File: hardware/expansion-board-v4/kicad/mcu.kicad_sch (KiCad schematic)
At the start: 28 parts, among them J4 USB-C_16P, SW1 RESET短接焊盘, SW2 BOOTSEL短接焊盘, U8 RP2040, U9 W25Q128JVSIQ, Y1 12MHz

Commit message: feat(hw): 删掉 TP1-7 与 SW1，飞线交叉 834→612、B 面中间让给电池
判据不是「省地方」，是这 7 条网络除了测试点没有第三方节点：
DEMOD0-3(GPIO20-23) 和 RECOVERED_CLK(GPIO24) 是固件里 PIO 解码状态机
往外**输出**的调试信号，不在接收链上——接收链是
AD8319 → TLV3501 比较器 → PULSES → GPIO19，一个测试点都没有。

固件调试在已打样的 v3.2 上做，那块板的 TP 和解调链与本板逐条相同
（expansion-board-v3/tools/sheet_mcu.py:95）。刷机走 USB UF2，
SWD 不是烧录必需。

SW1(RESET) 一并删掉：RUN 脚由 R5 上拉即可，复位靠断电或软件。

保留 SW2 并已搬到 U8 与 U9 之间——它是唯一的强制刷机入口，而且挂在
QSPI_SS 这条 RP2040 到 Flash 的片选线上，原来在 x52.8 等于给总线挂了
36mm stub（QSPI_SCLK 全长才 7.4mm），现在 6.1mm。

  飞线总长  3100 → 2640mm  (-15%)
  飞线交叉   834 → 612 处  (-27%)
  元件数     182 → 174
  B 面中间   完整让给电池 955465 (65x54)

GPIO20-24 的网络名保留在引脚映射表里没标 NC，将来要加回测试点补一句
s.place 即可，原理图上也还看得出这几个脚的预期用途。

验收：DRC error 0 条，F 面丝印全通过，原理图与 PCB 元件集合一致
（差集只有 H1-H4 螺丝孔），覆铜已重填。
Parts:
- removed SW1: RESET短接焊盘, Jumper:SolderJumper-2_P1.3mm_Open_Pad1.0x1.5mm, symbol Jumper:SolderJumper_2_Open
- removed TP1, TP2, TP3, TP4, TP5, TP6, TP7: TestPoint, TestPoint:TestPoint_Pad_1.0x1.0mm, symbol Connector:TestPoint

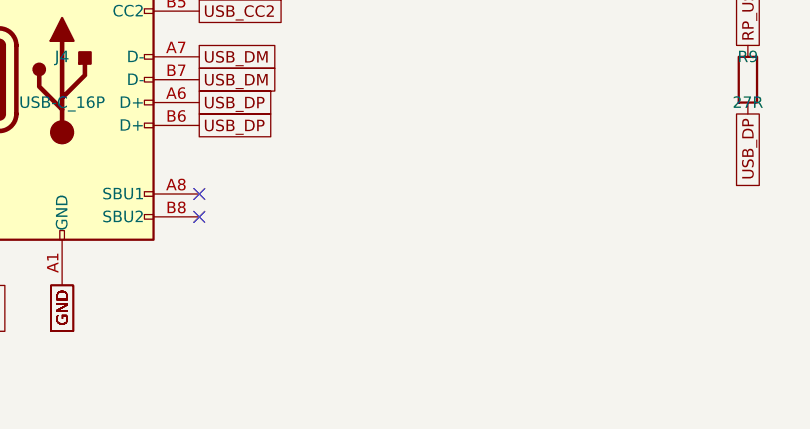
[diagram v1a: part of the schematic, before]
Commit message: feat(hw): 实现「单面可用」——J4 移 F 面、补 CC 下拉、电源电容改封装
## 单面可用是保底

不带电源版的 B 面现在**零贴装件**，可以走嘉立创经济型单面（¥267.1），
不必被迫上标准型双面（¥614.96）。上一版把 J4 留在 B 面，等于不带电源版
还是双面，只省 ¥35，白做。

三个改动：

  J4 (USB-C) → F 面 (144.63,73.00) rot=0
      courtyard 右沿贴齐板边 150，开口仍朝 +X（与微雪 H1 同侧）。
      翻面会镜像 x 且 USB-C 封装原点不在几何中心，x 是重新解出来的。
      USB_DP/DM 连的 R9/R10 本来就在 F 面 x117，搬过去走线反而更短；
      USB_CC1/2 与 USB_VBUS 只有带电源版才用，跨面过孔即可。

  新增 R7/R8（5.1k CC 下拉）→ F 面，紧邻 J4 2.2mm
      不带电源版没有 CH224K，CC 悬空则主机根本不认设备——USB-C 规范要求
      device 端呈现 Rd 才会被检测和枚举，不枚举就没法 UF2 刷机。
      **与 CH224K 二选一**，带电源版不贴。

  R37 (138.80,69.84) → (137.75,70.75)
      J4 的通孔安装脚穿到 B 面，落进了 R37 的 courtyard（DRC 报
      pth_inside_courtyard）。顺带把它到 CH224K CFG1 脚的距离 2.97→2.56mm。

## 电源电容改封装

不是为散热——电阻功率算过，最大的 R43 也才 (9−3.3)²/1k = 32.5mW，
0603 有 3 倍余量。真正的理由是两条：

  C72  6.8µF/25V  0603 → 1206
      接 PD 诱骗后的 9V 侧，耐压不能降。而 0603 在 25V 档容值上限只有
      1~2.2µF，6.8µF/25V 根本买不到。换封装后原位撞 C80，已就近重贴
      （按「离同网芯片引脚最近」而不是「离原位最近」找的位）。

  C73/C74/C75  10µF  0603 → 0805
      直流偏置下的容值衰减：10µF/16V X5R 在 5V 偏压下，0603 只剩
      3~4µF(−60%)，0805 还有 6~7µF(−30%)，直接影响输出纹波。

## 新增电源采购 CSV（单独一份，不混进整板 xlsx）

tools/gen_power_csv.py → BOM_电源采购_淘宝.csv，22 种料 / 30 颗。
按「卖家怎么找货」分组，同规格合并给总数，备注写清耐压/精度/为什么
封装不能换，末尾附两个版本的贴装差异。整板 88 料号的 xlsx 发给卖家太乱。

验收：DRC error 0 条，F 面丝印全通过，原理图↔PCB 零不一致，
176 元件已固化，全套文档重生成（BOM 88 料号 / SMT 79 料号 164 贴片位）。
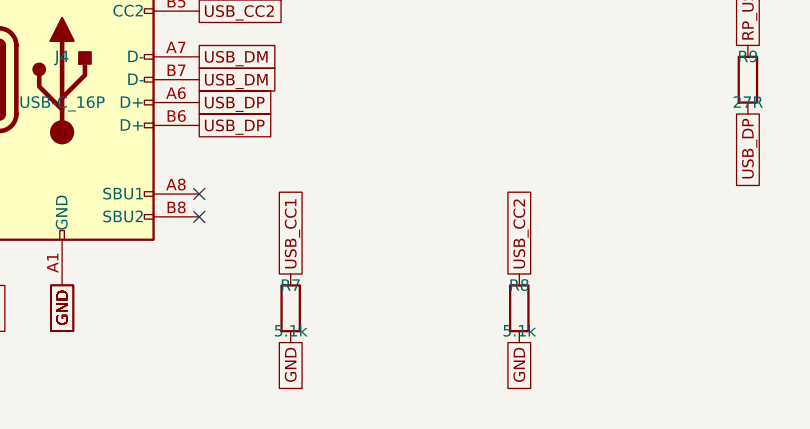
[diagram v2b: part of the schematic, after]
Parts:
- added R7, R8: 5.1k, Resistor_SMD:R_0603_1608Metric, symbol Device:R
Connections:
- net GND: now also R7.2, R8.2
- net USB_CC1: now also R7.1
- net USB_CC2: now also R8.1
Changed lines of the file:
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@@
+	(symbol
+		(lib_id "Device:R")
+		(at 88.9 215.9 0)
+		(unit 1)
+		(exclude_from_sim no)
+		(in_bom yes)
+		(on_board yes)
+		(dnp no)
+		(property "Reference" "R7"
+			(at 88.9 213.36 0)
+			(effects (font (size 1.27 1.27)))
+		)
+		(property "Value" "5.1k"
+			(at 88.9 218.44 0)
+			(effects (font (size 1.27 1.27)))
+		)
+		(property "Footprint" "Resistor_SMD:R_0603_1608Metric"
+			(at 88.9 220.98 0)
+			(effects (font (size 1.27 1.27))
+				(hide yes))
+		)
+		(property "Datasheet" "~"
+			(at 88.9 223.52 0)
+			(effects (font (size 1.27 1.27))
+				(hide yes))
+		)
+		(pin "1"
+		)
+		(pin "2"
+		)
+		(instances
+			(project "expansion-board-v4"
+				(path "/10000000-0000-4000-8000-000000000001/20000000-0000-4000-8000-000000000002"
+					(reference "R7")
+					(unit 1)
+				)
+			)
+		)
+	)
+	(global_label "USB_CC1"
+		(shape passive)
+		(at 88.9 212.09 270)
+		(effects (font (size 1.27 1.27)) (justify left))
+	)
+	(global_label "GND"
+		(shape passive)
+		(at 88.9 219.71 90)
+		(effects (font (size 1.27 1.27)) (justify right))
+	)
+	(symbol
+		(lib_id "Device:R")
+		(at 114.3 215.9 0)
+		(unit 1)
+		(exclude_from_sim no)
+		(in_bom yes)
+		(on_board yes)
+		(dnp no)
+		(property "Reference" "R8"
+			(at 114.3 213.36 0)
+			(effects (font (size 1.27 1.27)))
+		)
+		(property "Value" "5.1k"
+			(at 114.3 218.44 0)
+			(effects (font (size 1.27 1.27)))
+		)
+		(property "Footprint" "Resistor_SMD:R_0603_1608Metric"
+			(at 114.3 220.98 0)
+			(effects (font (size 1.27 1.27))
+				(hide yes))
+		)
+		(property "Datasheet" "~"
+			(at 114.3 223.52 0)
+			(effects (font (size 1.27 1.27))
+				(hide yes))
+		)
+		(pin "1"
+		)
+		(pin "2"
+		)
+		(instances
+			(project "expansion-board-v4"
+				(path "/10000000-0000-4000-8000-000000000001/20000000-0000-4000-8000-000000000002"
+					(reference "R8")
+					(unit 1)
+				)
+			)
+		)
+	)
+	(global_label "USB_CC2"
+		(shape passive)
+		(at 114.3 212.09 270)
+		(effects (font (size 1.27 1.27)) (justify left))
+	)
+	(global_label "GND"
+		(shape passive)
+		(at 114.3 219.71 90)
+		(effects (font (size 1.27 1.27)) (justify right))
+	)
 	(symbol
 		(lib_id "Device:R")

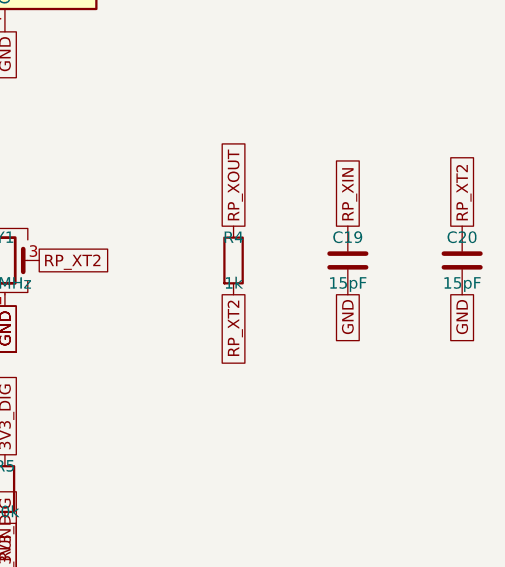
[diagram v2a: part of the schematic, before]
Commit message: fix(v4): 晶振负载电容按实测 CL 重算——C19/C20→33pF，C68/C69→18pF
罩哥给出实际买到的三颗晶振型号，CL 全部查实：

    Y1  X322512MSB4SI              CL=20pF     立创/JLCPCB/Evelta 三处一致
    Y2  ABM8W-48.0000MHZ-7-D1X-T3  CL=7pF      型号里的「-7-」就是 CL
    Y3  Q13FC13500004 (FC-135)     CL=12.5pF   Epson 官方 IC 配套页

按 C = (CL − Cstray) × 2、Cstray 取 3pF 重算：

              原值          新值      原偏差              新偏差
    C19/C20   15/15pF   →   33/33pF   -9.50pF ≈ 95ppm    -0.50pF ≈ 5ppm
    C68/C69   12/15pF   →   18/18pF   -2.83pF ≈ 28ppm    -0.50pF ≈ 5ppm
                            ↑ 原值还**不对称**，降低起振裕度

Y3 的 28ppm ≈ RTC 每天走时差 2.4 秒；改后 0.43 秒。
Y1 的 95ppm 虽在 USB 全速 ±500ppm 内，但计时精度白损失一个数量级。
sheet_subghz.py 里原注释写着「32k 12/15pF 照抄」——就是照抄参考设计没算。

Y2 不需要外部负载电容（CC1312 片内电容阵列），但 CL=7pF 要在固件 CCFG 的
XOSC HF cap-array 里配，这是软件项，已在核对清单里标注。

## 验证过：Gerber 一个字节没变

value 字段在 F.Fab 层，位号在 F.Silkscreen 层，导出的 13 层不含 F.Fab。
逐文件比对（排除 CreationDate/ProjectId 等注释行）：
**15 个 Gerber/钻孔文件的图形指令完全一致，0 处差异**。已打样的文件不用重发。

## 🔴 顺带修了一个静默的缓存 bug

_fresh_netlist() 只比对顶层 expansion-board-v4.kicad_sch 的 mtime，
而元件都在 mcu/power/rf1090/sensors/subghz/interface 这些**子页**里。
改子页时顶层 mtime 不动 → 缓存判定"新鲜" → 拿旧网表出文档，**一声不吭**。

实测：子页改于 23:56，网表缓存停在 8-26 19:13，顶层原理图是 8-26 15:52
（比缓存还旧）。结果原理图和板子都更新了，BOM_PURCHASE.md 和 ASSEMBLY.md
却还印着 12pF/15pF。

改成比对**所有 .kicad_sch 的最新 mtime**。四个脚本都有这个函数，一并修了。
这跟 2026-08-23 那次 /tmp 缓存是同一类问题的第二种形态——上次修了"只判存在性
不判时间戳"，这次是"判了时间戳但判错了对象"。

gen_bom.py 的 PARTS 断言拦住了新值未归类，正是它该干的活。
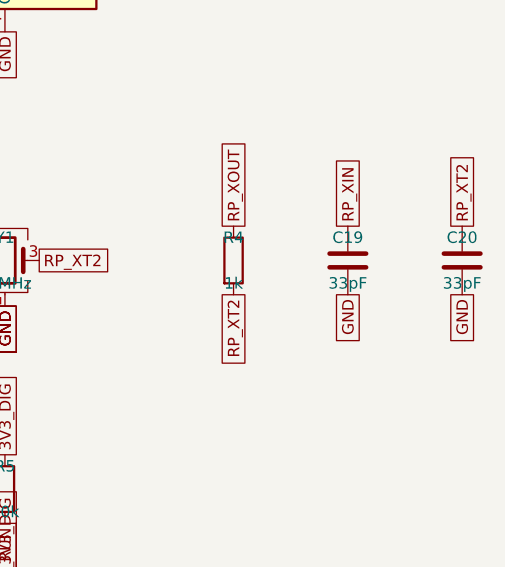
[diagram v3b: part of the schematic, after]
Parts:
- C19, C20: value 15pF -> 33pF
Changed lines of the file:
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@@
 			(effects (font (size 1.27 1.27)))
 		)
-		(property "Value" "15pF"
+		(property "Value" "33pF"
 			(at 228.6 116.84 0)
 			(effects (font (size 1.27 1.27)))
@@
 			(effects (font (size 1.27 1.27)))
 		)
-		(property "Value" "15pF"
+		(property "Value" "33pF"
 			(at 241.3 116.84 0)
 			(effects (font (size 1.27 1.27)))

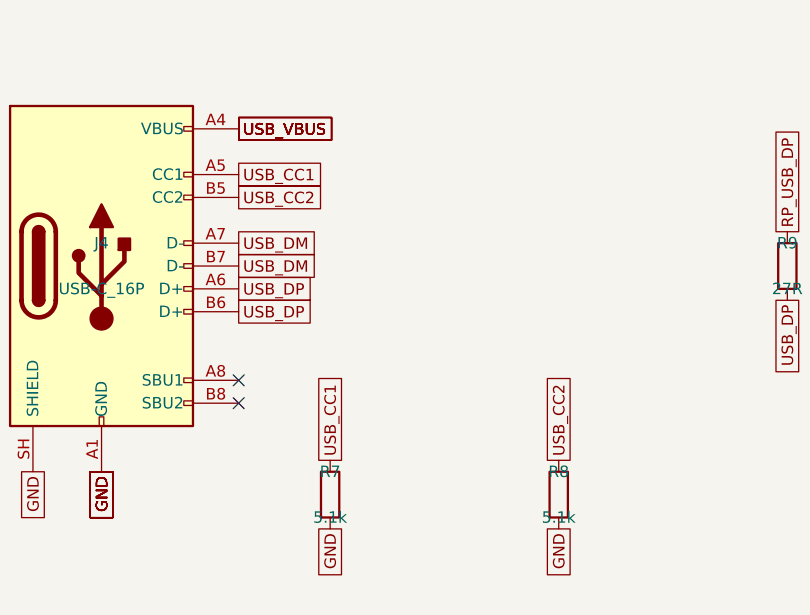
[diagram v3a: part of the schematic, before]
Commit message: fix(v4): correct RF and power networks for V4.2
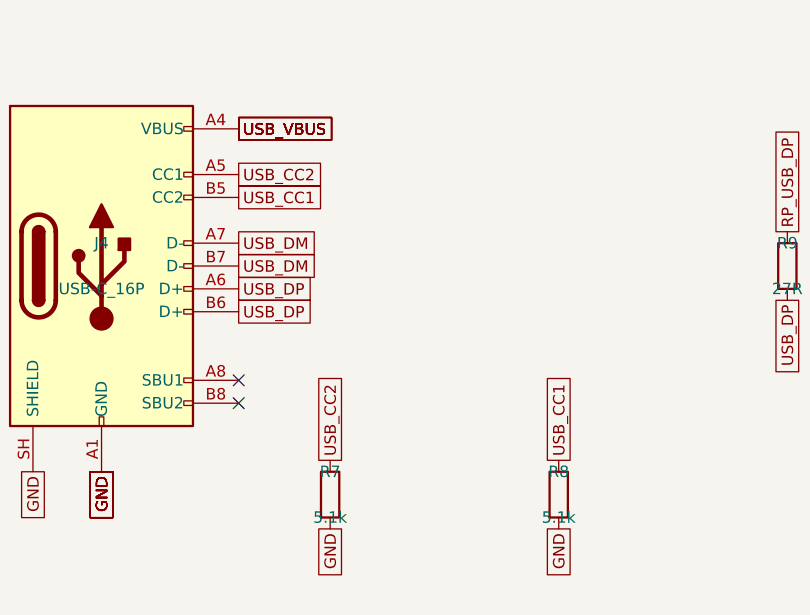
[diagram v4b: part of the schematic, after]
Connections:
- net USB_CC1: now also J4.B5 (CC2), R8.1; no longer J4.A5 (CC1), R7.1
- net USB_CC2: now also J4.A5 (CC1), R7.1; no longer J4.B5 (CC2), R8.1
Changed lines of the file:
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@@
 		(effects (font (size 1.27 1.27)) (justify right))
 	)
-	(global_label "USB_CC1"
+	(global_label "USB_CC2"
 		(shape passive)
 		(at 78.74 180.34 0)
 		(effects (font (size 1.27 1.27)) (justify left))
 	)
-	(global_label "USB_CC2"
+	(global_label "USB_CC1"
 		(shape passive)
 		(at 78.74 182.88 0)
@@
 		)
 	)
-	(global_label "USB_CC1"
+	(global_label "USB_CC2"
 		(shape passive)
 		(at 88.9 212.09 270)
@@
 		)
 	)
-	(global_label "USB_CC2"
+	(global_label "USB_CC1"
 		(shape passive)
 		(at 114.3 212.09 270)

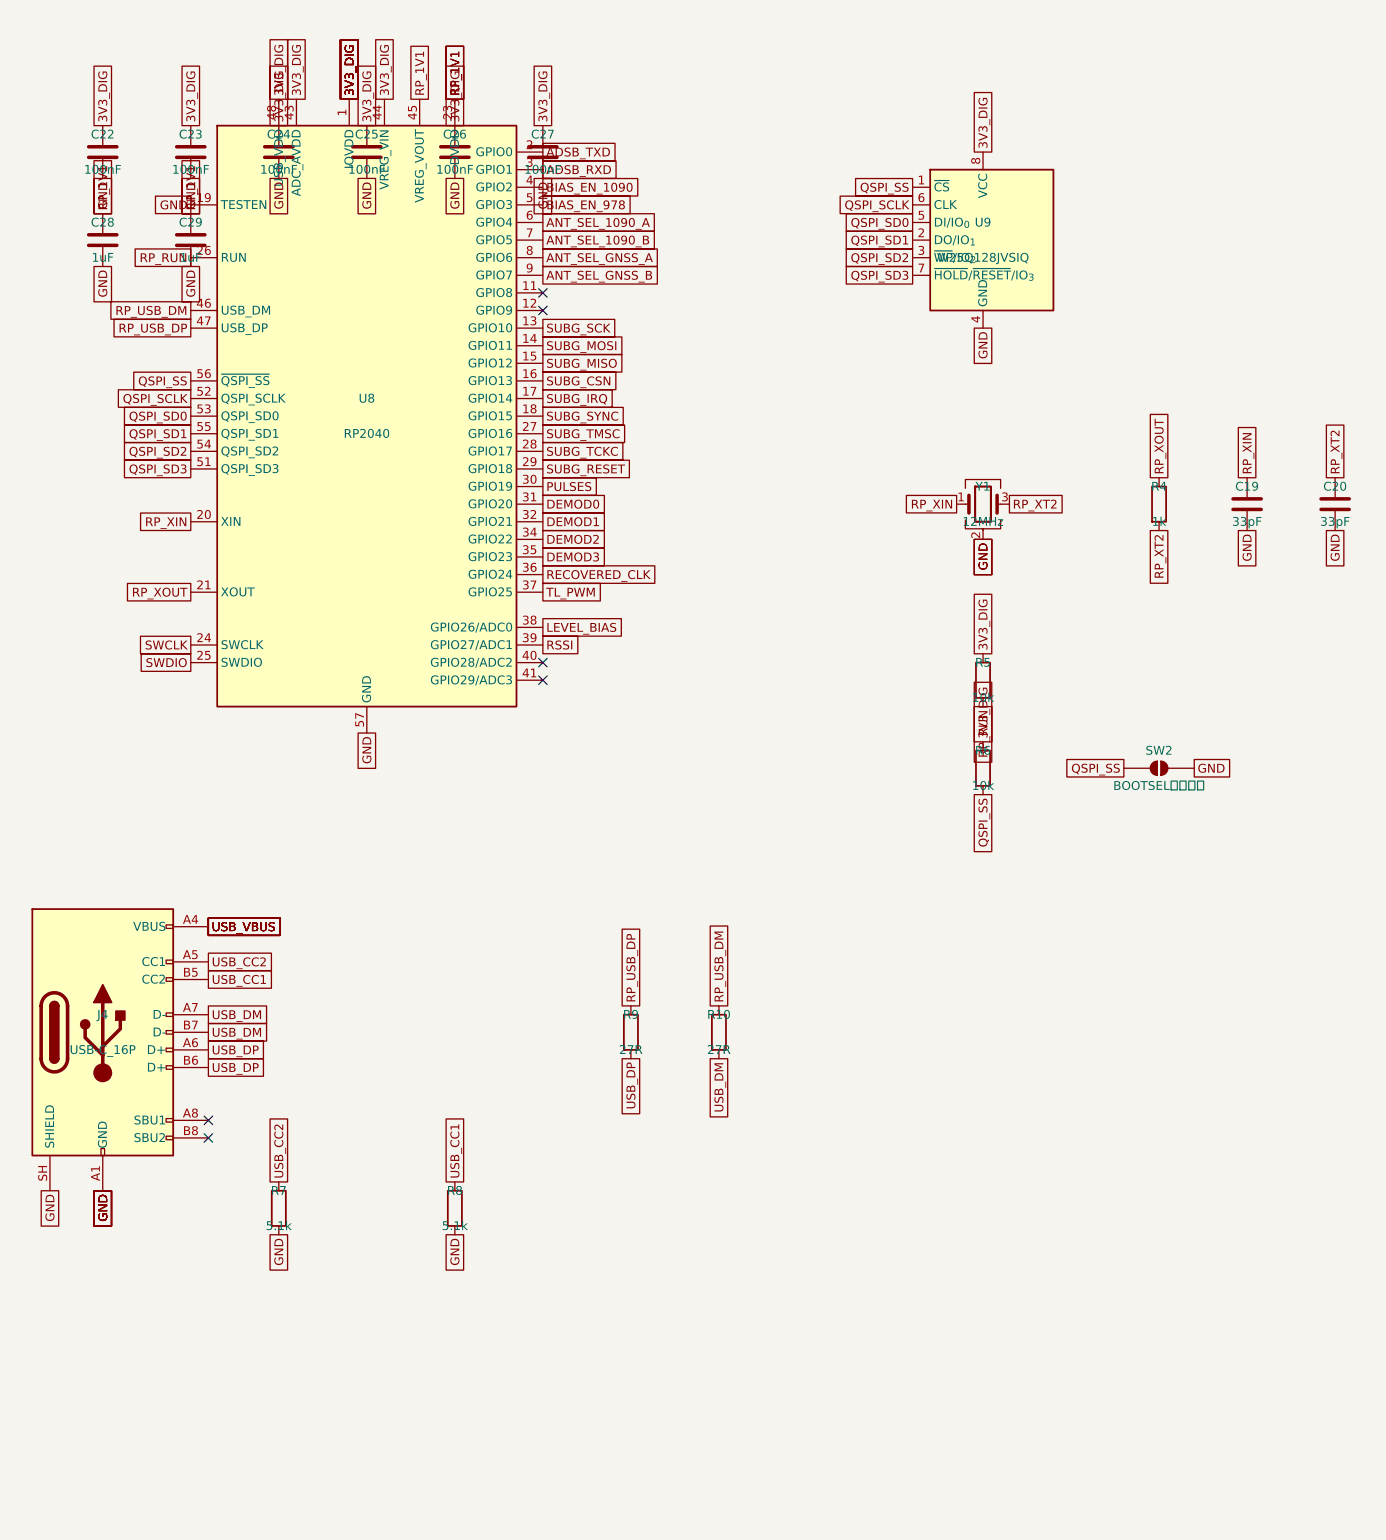
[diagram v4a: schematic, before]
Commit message: fix(v4): finalize V4.3 board after manual routing
罩哥手工完成全部布线后的定稿。DRC 0 violations / 0 unconnected。

板子本身:
- 1607 段走线 / 415 个过孔 / 207 个封装 / 15 个 zone
- RP_1V1 在 B.Cu 合并为单块 228.96mm2，四颗 RP_1V1 去耦落入其中
- C81 挪到 U12 旁 1.47mm(原 3.36mm)，脚下由「无铜」变为落在 B.Cu 的 3V3_RF 上
- U8.23(DVDD) 补一个 RP_1V1 过孔 @(85.798,72.600)，接入距离 1.63 -> 0.88mm
  落点在既有走线上，未改任何走线；与相邻 QFN 焊盘边缘间距 +0.312mm

原理图:
- rf1090 的 PWR_FLAG 由 #FLG05 改为 #FLG06。sheet_power.py 已占用 #FLG05,
  两页撞号会让网表导出报「批注错误」。改后网表 714 节点、网络归属零变化。

.kicad_pro 保留正式板原有的 FINE netclass(0.13mm, 用于 DEMOD0-3/RECOVERED_CLK/
SWCLK/SWDIO)。板上这 7 个网络实际都按 0.15mm 布线、FINE 处于闲置; 两份工程
文件下各跑一次 DRC 均为 0，且 drc_exclusions 都是空的。
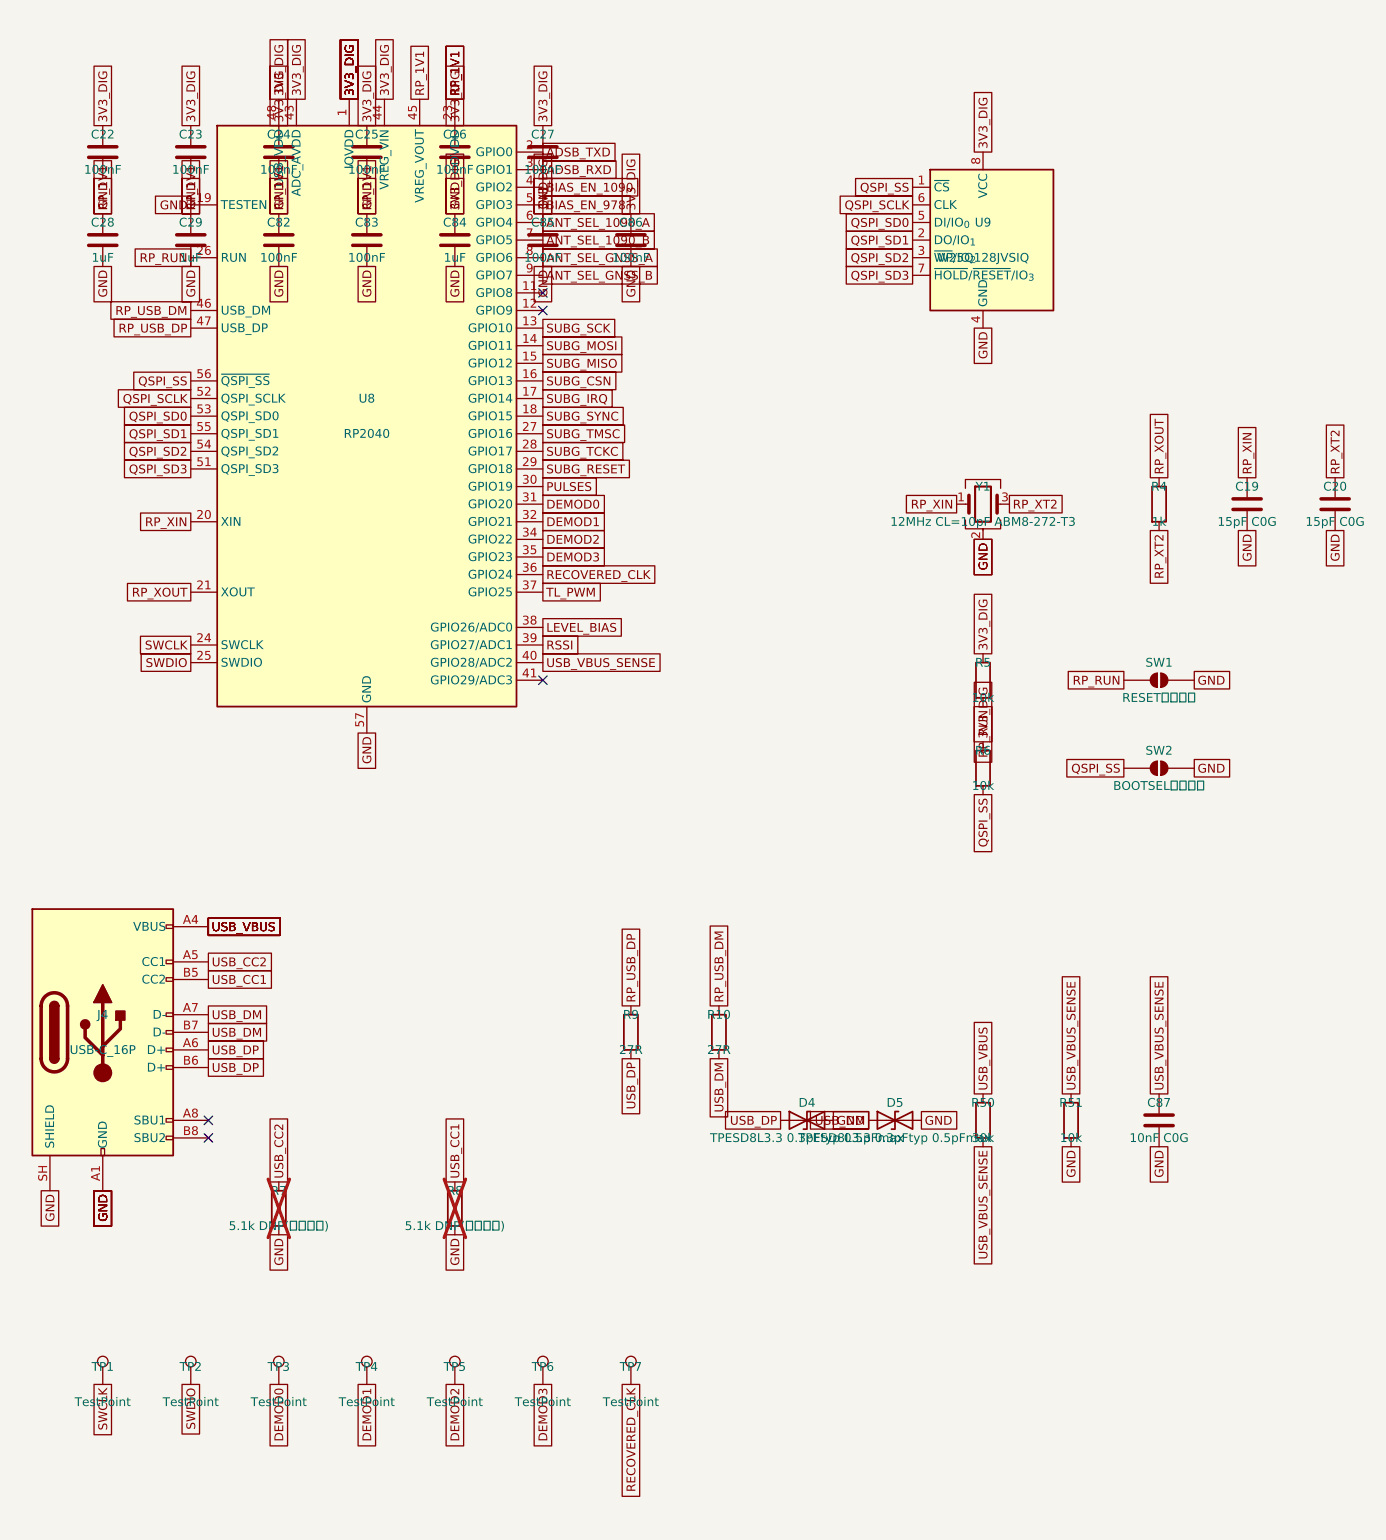
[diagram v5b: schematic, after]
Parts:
- added C82, C83, C85, C86: 100nF, Capacitor_SMD:C_0603_1608Metric, symbol Device:C
- added C84: 1uF, Capacitor_SMD:C_0603_1608Metric, symbol Device:C
- added C87: 10nF C0G, Capacitor_SMD:C_0603_1608Metric, symbol Device:C
- added D4, D5: TPESD8L3.3 0.3pFtyp 0.5pFmax, Diode_SMD:D_0402_1005Metric, symbol Device:D_TVS
- added R50: 30k, Resistor_SMD:R_0603_1608Metric, symbol Device:R
- added R51: 10k, Resistor_SMD:R_0603_1608Metric, symbol Device:R
- added SW1: RESET短接焊盘, Jumper:SolderJumper-2_P1.3mm_Open_Pad1.0x1.5mm, symbol Jumper:SolderJumper_2_Open
- added TP1, TP2, TP3, TP4, TP5, TP6, TP7: TestPoint, TestPoint:TestPoint_Pad_1.0x1.0mm, symbol Connector:TestPoint
- C19, C20: value 33pF -> 15pF C0G
- R7, R8: value 5.1k -> 5.1k DNP(带电源版); now not fitted
- Y1: value 12MHz -> 12MHz CL=10pF ABM8-272-T3
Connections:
- net 3V3_DIG: now also C84.1, C85.1, C86.1
- net DEMOD0: now also TP3.1
- net DEMOD1: now also TP4.1
- net DEMOD2: now also TP5.1
- net DEMOD3: now also TP6.1
- net GND: now also C82.2, C83.2, C84.2, C85.2, C86.2, C87.2, D4.2 (A2), D5.2 (A2), R51.2, SW1.2 (B)
- net RECOVERED_CLK: now also TP7.1
- net RP_1V1: now also C82.1, C83.1
- net RP_RUN: now also SW1.1 (A)
- net SWCLK: now also TP1.1
- net SWDIO: now also TP2.1
- net USB_DM: now also D5.1 (A1)
- net USB_DP: now also D4.1 (A1)
- net USB_VBUS: now also R50.1
- net USB_VBUS_SENSE: now reaches U8.40 (GPIO28/ADC2)
- net USB_VBUS_SENSE: now also C87.1, R50.2, R51.1
- no-connect marks 6 -> 5
